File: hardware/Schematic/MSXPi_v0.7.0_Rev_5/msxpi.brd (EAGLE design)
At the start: 101 x 64.7 mm, 36 parts, among them IC1 LD117AS33TR

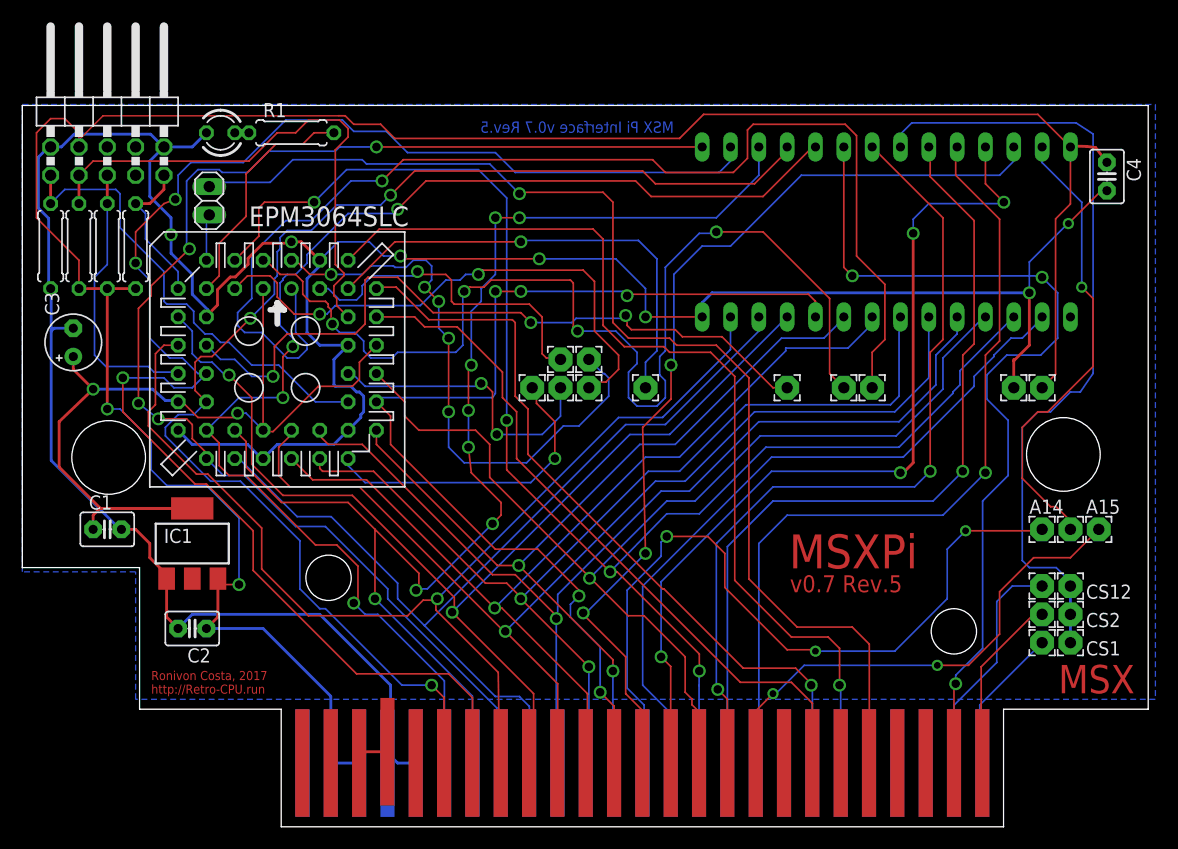
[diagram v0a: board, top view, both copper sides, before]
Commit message: Schema update: added jumper to disable Rapsberry Pi VCC
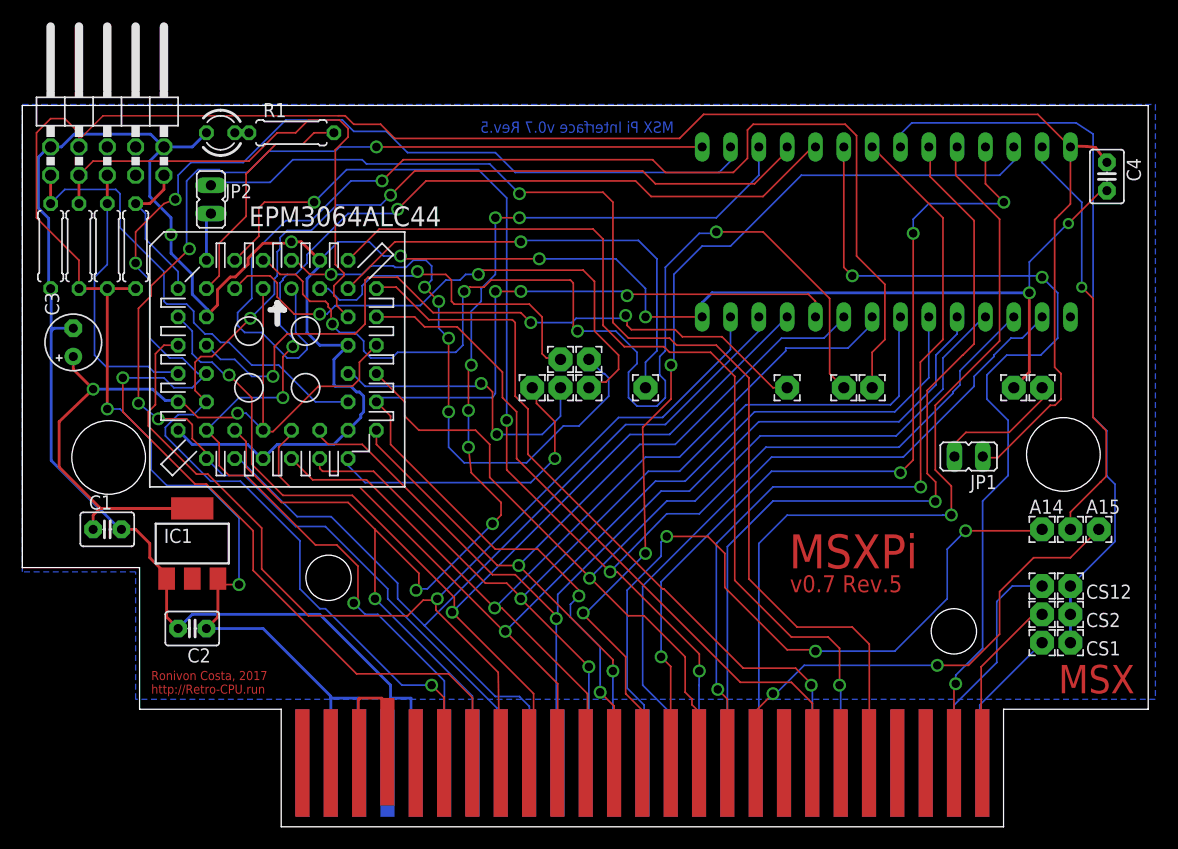
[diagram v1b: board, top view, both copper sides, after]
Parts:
- removed JP5: (no value), pinhead:1X02
- added JP1, JP2: (no value), jumper:JP1
- renumbered EPM3064SLC to EPM3064ALC44
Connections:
- new net N$3: +5V.1, JP1.2
- net +5V: now also JP1.1; no longer +5V.1
- net BUSDIR: now also JP2.1; no longer JP5.1
- net MSXR1: now also JP2.2; no longer JP5.2
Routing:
- net +5V: track 210.6 -> 226.1 mm
- net N$3: track 0.00 -> 11.7 mm
- net N$2: track 3.73 -> 13.3 mm
- net GND: track 263.1 -> 268.5 mm
- net ROM_OE: track 71.6 -> 67.4 mm
- net ROM_A14: track 41.4 -> 38.0 mm
- net A9: track 74.2 -> 75.8 mm
- net A11: track 74.5 -> 75.3 mm
